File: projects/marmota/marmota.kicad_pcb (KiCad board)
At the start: 4 copper layers, 70 x 70 mm, 20 parts, among them J1 USB_C, J2 Conn_01x20_Pin, J3 Conn_01x20_Pin, J4 TC2030-NL, J5 Conn_01x04_MountingPin, J6 Conn_01x04_MountingPin, SW1 Button top, SW2 Button side, U6 nRF52840_E73-2G4M08S1C, U7 nPM1300-QEXX

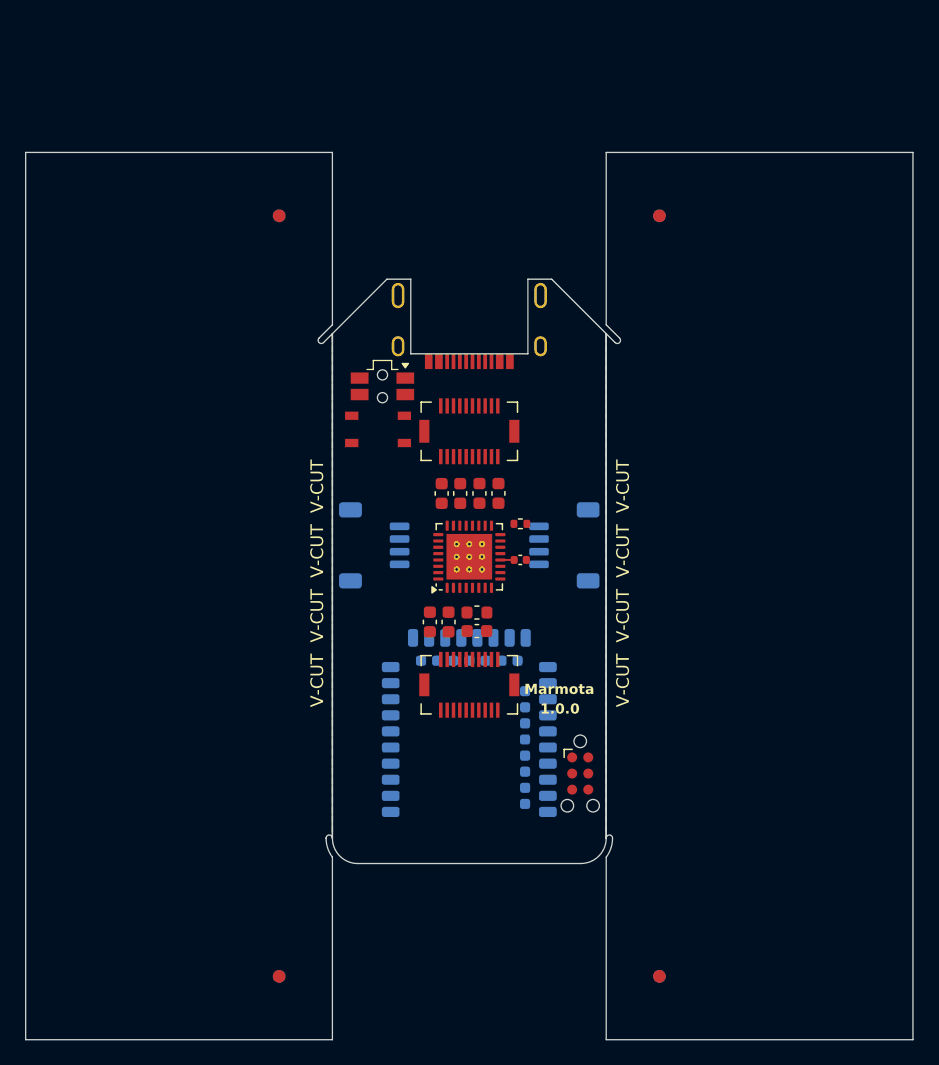
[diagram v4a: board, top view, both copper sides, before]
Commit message: Updated for nRF52840
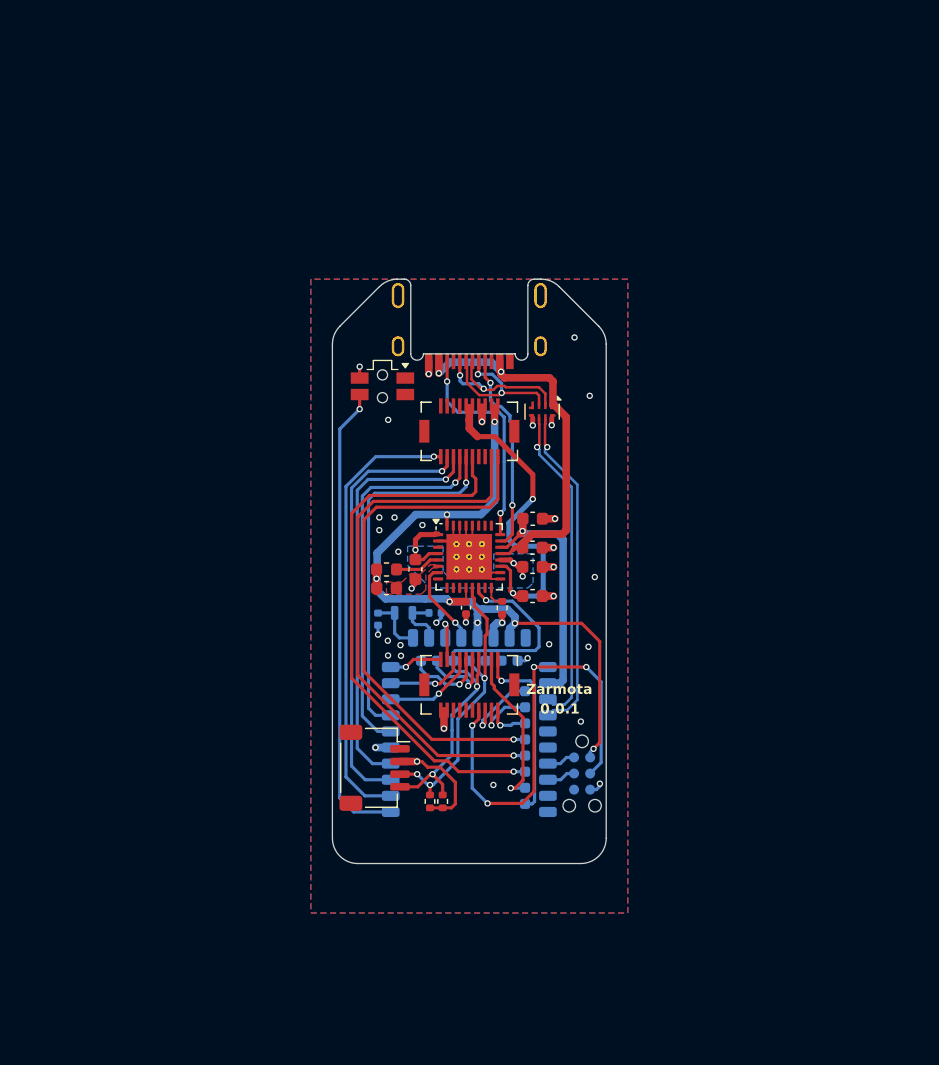
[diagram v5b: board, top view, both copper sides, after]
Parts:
- removed C8: 10uF, Capacitor_SMD:C_0603_1608Metric
- removed J5: Conn_01x04_MountingPin, Connector_JST:JST_SH_SM04B-SRSS-TB_1x04-1MP_P1.00mm_Horizontal
- removed SW1: Button top, ILO_fp:Alpsalpine_SKRP_compact
- added C1: 12pF, Capacitor_SMD:C_0402_1005Metric, B.Cu at (57.3, 66.3)
- added C2: 12pF, Capacitor_SMD:C_0402_1005Metric, B.Cu at (52.8, 66.8)
- added R1: 5.1kR, Resistor_SMD:R_0402_1005Metric, F.Cu at (56.9, 81.2)
- added R2: 5.1kR, Resistor_SMD:R_0402_1005Metric, F.Cu at (57.9, 81.2)
- added U1: ECMF02-4CMX8, hlord2000-Package_DFN_QFN:ST_UQFN-8L_1.2x2.5mm_P0.5mm, F.Cu at (65.8, 50.5)
- added Y1: 32.768KHz, Crystal:Crystal_SMD_2012-2Pin_2.0x1.2mm, B.Cu at (54.8, 66.3)
- J4: moved to B.Cu
- J6: moved to F.Cu
- moved J6 17.6 mm to (52.5, 78.5), turned to -90 degrees
- moved C12 8.53 mm to (65.0, 65.0), turned to 0 degrees
- moved L1 7.90 mm to (53.5, 62.9)
- moved C11 7.89 mm to (53.5, 64.4)
- moved C10 7.45 mm to (65.0, 58.9), turned to 0 degrees
- moved C6 7.16 mm to (65.0, 62.7), turned to 0 degrees
- moved C9 7.13 mm to (65.0, 61.2), turned to 0 degrees
- moved R5 6.78 mm to (62.6, 65.9), turned to -90 degrees
- moved C5 5.70 mm to (59.7, 65.9), turned to -90 degrees
- moved C7 4.90 mm to (55.8, 62.9)
- moved J4 0.15 mm to (68.9, 79.0)
- turned U7 to 0 degrees
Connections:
- net /BAT+ renamed VBAT
- net /GP13 renamed /TOUCH_MEAS
- J1 pad A6: /USB_D+ -> /D+
- J1 pad A7: /USB_D- -> /D-
- J1 pad B6: /USB_D+ -> /D+
- J1 pad B7: /USB_D- -> /D-
- J2 pad 11: /GP4 -> /IMU0_~{CS}
- J2 pad 12: /GP5 -> /IMU1_~{CS}
- J2 pad 13: /GP6 -> /IMU0_~{INT}
- J2 pad 14: /GP7 -> /IMU1_~{INT}
- J2 pad 15: /GP8 -> /SCROLL_A
- J2 pad 16: /GP9 -> /SCROLL_B
- J2 pad 19: /GP12 -> /TOUCH_STIM
- J3 pad 1: /ADC3 -> /LSTICK_Y
- J3 pad 18: /SPI_RX -> /SPI_SDO
- J3 pad 19: /SPI_TX -> /SPI_SDI
- J3 pad 2: /ADC2 -> /LSTICK_X
- J3 pad 20: /SPI_CLK -> /SPI_SCK
- J3 pad 3: /ADC1 -> /RSTICK_Y
- J3 pad 4: /ADC0 -> /RSTICK_X
- J3 pad 5: /GP25 -> /EXP0_~{INT}
- J3 pad 6: /GP24 -> /EXP1_~{INT}
- J6 pad 1: unconnected-(J6-Pin_1-Pad1) -> GND
- J6 pad 2: unconnected-(J6-Pin_2-Pad2) -> VDD
- J6 pad 3: unconnected-(J6-Pin_3-Pad3) -> /I2C_SDA
- J6 pad 4: unconnected-(J6-Pin_4-Pad4) -> /I2C_SCL
- J6 pad MP: unconnected-(J6-MountPin-PadMP) -> GND
- SW2 pad 1: unconnected-(SW2-Pad1) -> GND
- SW2 pad 2: unconnected-(SW2-Pad2) -> /SW1
- U6 pad 1: /GP11 -> /SW1
- U6 pad 10: /UART0_RX -> /LSTICK_Y
- U6 pad 12: unconnected-(U6-P0.26-Pad12) -> /EXP0_~{INT}
- U6 pad 14: /GP25 -> /EXP1_~{INT}
- U6 pad 15: /ADC3 -> /LSTICK_X
- U6 pad 17: /GP9 -> /NPM1300.INT
- U6 pad 18: /ADC2 -> /I2C_SDA
- U6 pad 2: /GP10 -> /IMU0_~{CS}
- U6 pad 20: /I2C_SDA -> unconnected-(U6-P0.12-Pad20)
- U6 pad 22: /GP24 -> unconnected-(U6-P0.07-Pad22)
- U6 pad 28: /UART1_TX -> /SPI_SDO
- U6 pad 3: /ADC1 -> /IMU1_~{CS}
- U6 pad 30: /SPI_RX -> /SPI_SDI
- U6 pad 32: /SPI_TX -> /SPI_SCK
- U6 pad 33: /UART1_RX -> unconnected-(U6-P0.13-Pad33)
- U6 pad 34: /SPI_CLK -> unconnected-(U6-P0.22-Pad34)
- U6 pad 36: /GP5 -> unconnected-(U6-P1.00-Pad36)
- U6 pad 38: /GP6 -> unconnected-(U6-P1.02-Pad38)
- U6 pad 4: /GP4 -> /IMU0_~{INT}
- U6 pad 40: /GP7 -> /UART1_RX
- U6 pad 42: /GP8 -> /UART1_TX
- U6 pad 6: /GP12 -> /IMU1_~{INT}
- U6 pad 7: /ADC0 -> /SCROLL_A
- U6 pad 8: /UART0_TX -> /RSTICK_X
- U6 pad 9: /NPM1300.INT -> /RSTICK_Y
- U7 pad 13: /NPM1300.SDA -> /I2C_SDA
- U7 pad 14: /NPM1300.SCL -> /I2C_SCL
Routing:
- net VDD: track 1.09 -> 84.6 mm, vias 0 -> 8
- net /SCROLL_B: track 0.00 -> 43.1 mm, vias 0 -> 1
- net /TOUCH_STIM: track 0.00 -> 42.6 mm, vias 0 -> 1
- net /TOUCH_MEAS: track 0.00 -> 41.5 mm, vias 0 -> 1
- net /SW1: track 0.00 -> 37.0 mm, vias 0 -> 1
- net GND: track 0.00 -> 36.6 mm, vias 0 -> 35
- net /RUN: track 0.00 -> 36.4 mm, vias 0 -> 4
- net /IMU0_~{CS}: track 0.00 -> 35.5 mm, vias 0 -> 1
- net /IMU1_~{CS}: track 0.00 -> 34.5 mm, vias 0 -> 1
- net /I2C_SCL: track 0.00 -> 34.2 mm, vias 0 -> 3
- net /IMU0_~{INT}: track 0.00 -> 32.9 mm, vias 0 -> 1
- net Net-(U1-VBUS): track 0.00 -> 30.5 mm, vias 0 -> 2
- net /IMU1_~{INT}: track 0.00 -> 30.1 mm, vias 0 -> 1
- net /SCROLL_A: track 0.00 -> 28.9 mm, vias 0 -> 1
- net VBAT: track 0.00 -> 26.6 mm, vias 0 -> 2
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- added copper zone on B.Cu, net GND
- added copper zone on F.Cu, net GND
- added copper zone on In1.Cu, net GND
- added copper zone on In2.Cu, net GND
- added copper zone on B.Cu, net VSYS
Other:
- board size 70 x 70 mm -> 21.6 x 46.1 mm
- board text added: "0.0.1"
- board text added: "Input Labs Oy. Zarmota 0.0.1"
- board text added: "Zarmota"
- board text removed: "1.0.0"
- board text removed: "Input Labs Oy. Marmota 1.0.0"
- board text removed: "Marmota"
- board text removed: "V-CUT"
- board text removed: "V-CUT V-CUT V-CUT V-CUT"
